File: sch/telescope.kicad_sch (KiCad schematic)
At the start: 74 parts, among them J1 USB_B, J2 M1, J3 M2, J4 12V, J5 UART, Q1 MMBT3904, Q2 MMBT3904, Q3 MMBT3904, SW1 RST, SW2 IO0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

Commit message: split motor driver enable lines and increase motor trace width
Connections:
- net ~{M2_ENA}: now reaches U5.29 (IO5)
- net ~{M2_ENA}: now also U2.23 (~{ENABLE})
- net ~{M_ENA} renamed ~{M1_ENA}
- net ~{M1_ENA}: no longer U2.23 (~{ENABLE})
- no-connect marks 27 -> 26
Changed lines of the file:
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@@
-	)
-	(no_connect
-		(at 236.22 102.87)
 	)
 	(no_connect
@@
 		)
 	)
-	(label "~{M_ENA}"
+	(label "~{M1_ENA}"
 		(at 158.75 52.07 180)
 		(fields_autoplaced yes)
@@
 		)
 	)
+	(label "~{M2_ENA}"
+		(at 236.22 102.87 0)
+		(fields_autoplaced yes)
+		(effects
+			(font
+				(size 1.27 1.27)
+			)
+			(justify left bottom)
+		)
+	)
 	(label "LED"
 		(at 190.5 100.33 0)
@@
 		)
 	)
-	(label "~{M_ENA}"
+	(label "~{M1_ENA}"
 		(at 236.22 123.19 0)
 		(fields_autoplaced yes)
@@
 		)
 	)
-	(label "~{M_ENA}"
+	(label "~{M2_ENA}"
 		(at 231.14 52.07 180)
 		(fields_autoplaced yes)

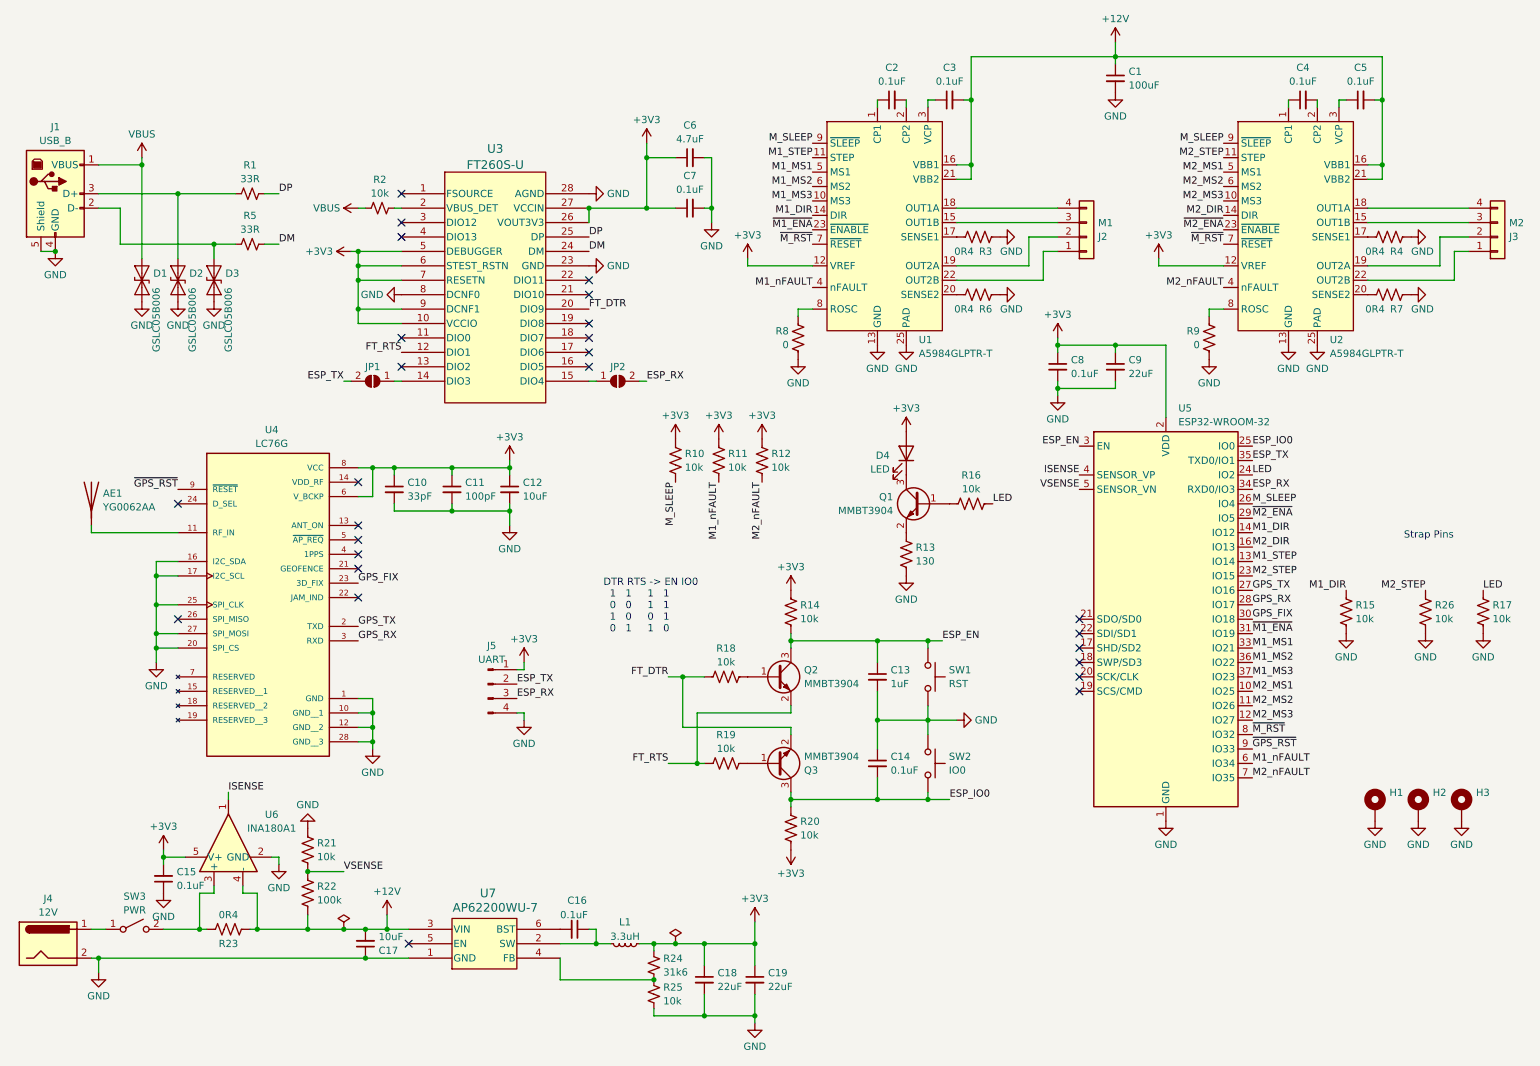
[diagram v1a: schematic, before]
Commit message: add overvolt protection, USB power, and GPO to schematics
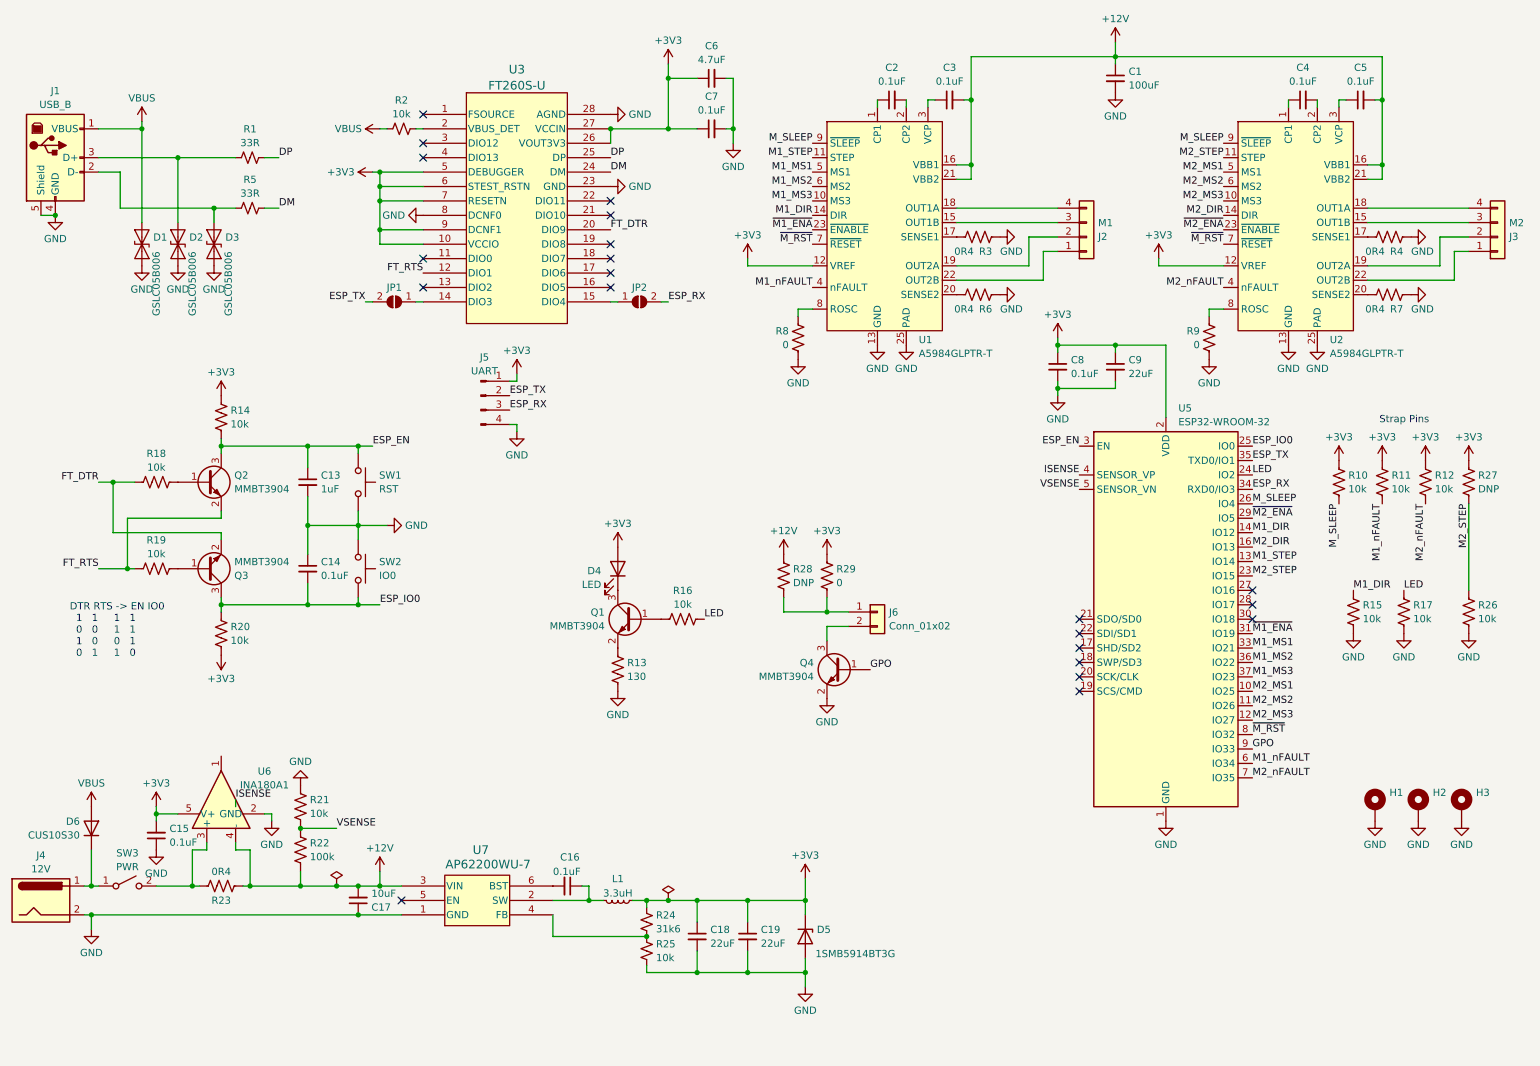
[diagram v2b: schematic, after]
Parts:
- removed AE1: YG0062AA, YG0062AA:XCVR_YG0062AA, symbol Device:Antenna
- removed C10: 33pF, Capacitor_SMD:C_0805_2012Metric_Pad1.18x1.45mm_HandSolder, symbol Device:C_Small
- removed C11: 100pF, Capacitor_SMD:C_0805_2012Metric_Pad1.18x1.45mm_HandSolder, symbol Device:C_Small
- removed C12: 10uF, Capacitor_SMD:C_0805_2012Metric_Pad1.18x1.45mm_HandSolder, symbol Device:C_Small
- removed U4: LC76G, LC76G:XCVR_LC76G, symbol LC76G:LC76G
- added D5: 1SMB5914BT3G, symbol Device:D_Zener
- added D6: CUS10S30, symbol Device:D
- added J6: Conn_01x02, symbol Connector_Generic:Conn_01x02
- added Q4: MMBT3904, Package_TO_SOT_SMD:SOT-23, symbol Transistor_BJT:MMBT3904
- added R27: DNP, Resistor_SMD:R_0805_2012Metric_Pad1.20x1.40mm_HandSolder, symbol Device:R_US
- added R28: DNP, symbol Device:R_US
- added R29: 0, symbol Device:R_US
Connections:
- net +12V: now also R28.1
- net +3V3: now also D5.1 (K), R27.2, R29.1
- net GND: now also D5.2 (A), Q4.2 (E)
- net ISENSE: no longer U6.1
- net M2_STEP: now also R27.1
- net VBUS: now also D6.2 (A)
- net at J4.1, SW3.1 (A): now also D6.1 (K)
- net GPS_FIX: no longer names the net of U5.30 (IO18)
- net GPS_RX: no longer names the net of U5.28 (IO17)
- net GPS_TX: no longer names the net of U5.27 (IO16)
- net ~{GPS_RST} renamed GPO
- net GPO: now also Q4.1 (B)
- new net: J6.1 (Pin_1), R28.2, R29.2
- new net: J6.2 (Pin_2), Q4.3 (C)
- no-connect marks 26 -> 21
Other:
- moved on the sheet: C13, C14, C15, C16, C17, C18, C19, C6, C7, D1, D2, D3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

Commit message: update pcb
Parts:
- removed R29: 0, symbol Device:R_US
- added JP3, JP4: SolderJumper_2_Open, Jumper:SolderJumper-2_P1.3mm_Open_TrianglePad1.0x1.5mm, symbol Jumper:SolderJumper_2_Open
- added RV1: R_Potentiometer_US, Potentiometer_SMD:Potentiometer_Bourns_TC33X_Vertical, symbol Device:R_Potentiometer_US
- added TP1: TestPoint, TestPoint:TestPoint_Pad_D1.5mm, symbol Connector:TestPoint
- D5: value 1SMB5914BT3G -> PDZ3.6B; footprint (none) -> Diode_SMD:D_SOD-323_HandSoldering
- D6: footprint (none) -> Diode_SMD:D_SOD-323_HandSoldering
- J6: footprint (none) -> Connector_PinHeader_2.54mm:PinHeader_1x02_P2.54mm_Vertical
- R28: value DNP -> 10k; footprint (none) -> Resistor_SMD:R_0805_2012Metric_Pad1.20x1.40mm_HandSolder
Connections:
- net +12V: now also JP3.2 (B); no longer R28.1
- net +3V3: now also JP4.2 (B), RV1.1; no longer U1.12 (VREF), U2.12 (VREF)
- net GND: now also RV1.3
- net GPO: now also R28.2, U5.27 (IO16); no longer Q4.1 (B), U5.9 (IO33)
- net ISENSE: now also U6.1
- net at J6.1 (Pin_1): now also JP3.1 (A), JP4.1 (A); no longer R28.2
- new net: RV1.2, TP1.1, U1.12 (VREF), U2.12 (VREF)
- new net: Q4.1 (B), R28.1
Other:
- moved on the sheet: C13, C14, D4, J5, J6, Q1, Q2, Q3, Q4, R13, R14, R16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

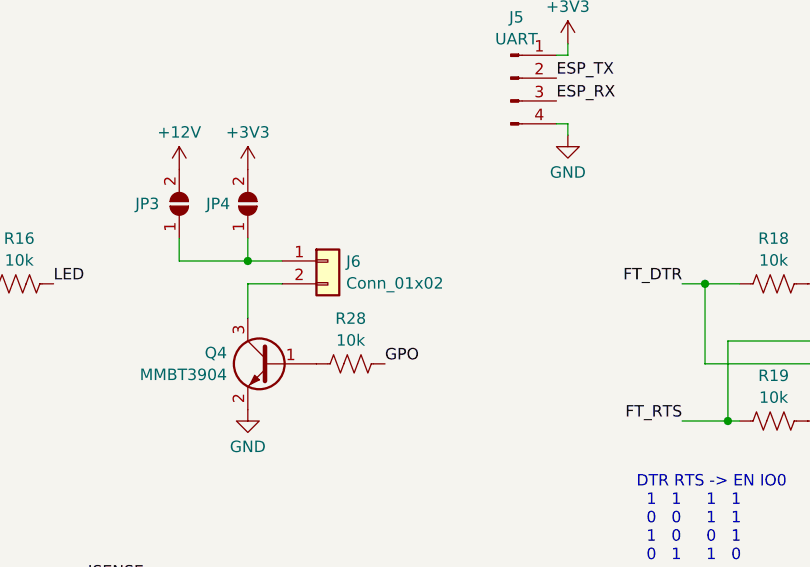
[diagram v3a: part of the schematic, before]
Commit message: switch to jst and generate v2 gerbers
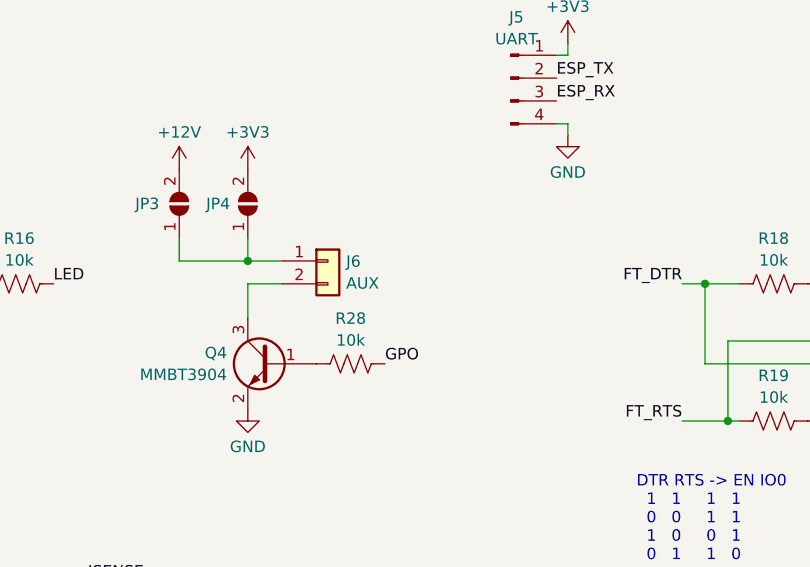
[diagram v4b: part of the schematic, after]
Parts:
- J6: value Conn_01x02 -> AUX; footprint Connector_PinHeader_2.54mm:PinHeader_1x02_P2.54mm_Vertical -> Connector_JST:JST_PH_B2B-PH-K_1x02_P2.00mm_Vertical
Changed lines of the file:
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@@
 			)
 		)
-		(property "Value" "Conn_01x02"
+		(property "Value" "AUX"
 			(at 83.312 110.4321 0)
 			(effects
@@
 			)
 		)
-		(property "Footprint" "Connector_PinHeader_2.54mm:PinHeader_1x02_P2.54mm_Vertical"
+		(property "Footprint" "Connector_JST:JST_PH_B2B-PH-K_1x02_P2.00mm_Vertical"
 			(at 81.28 107.95 0)
 			(effects

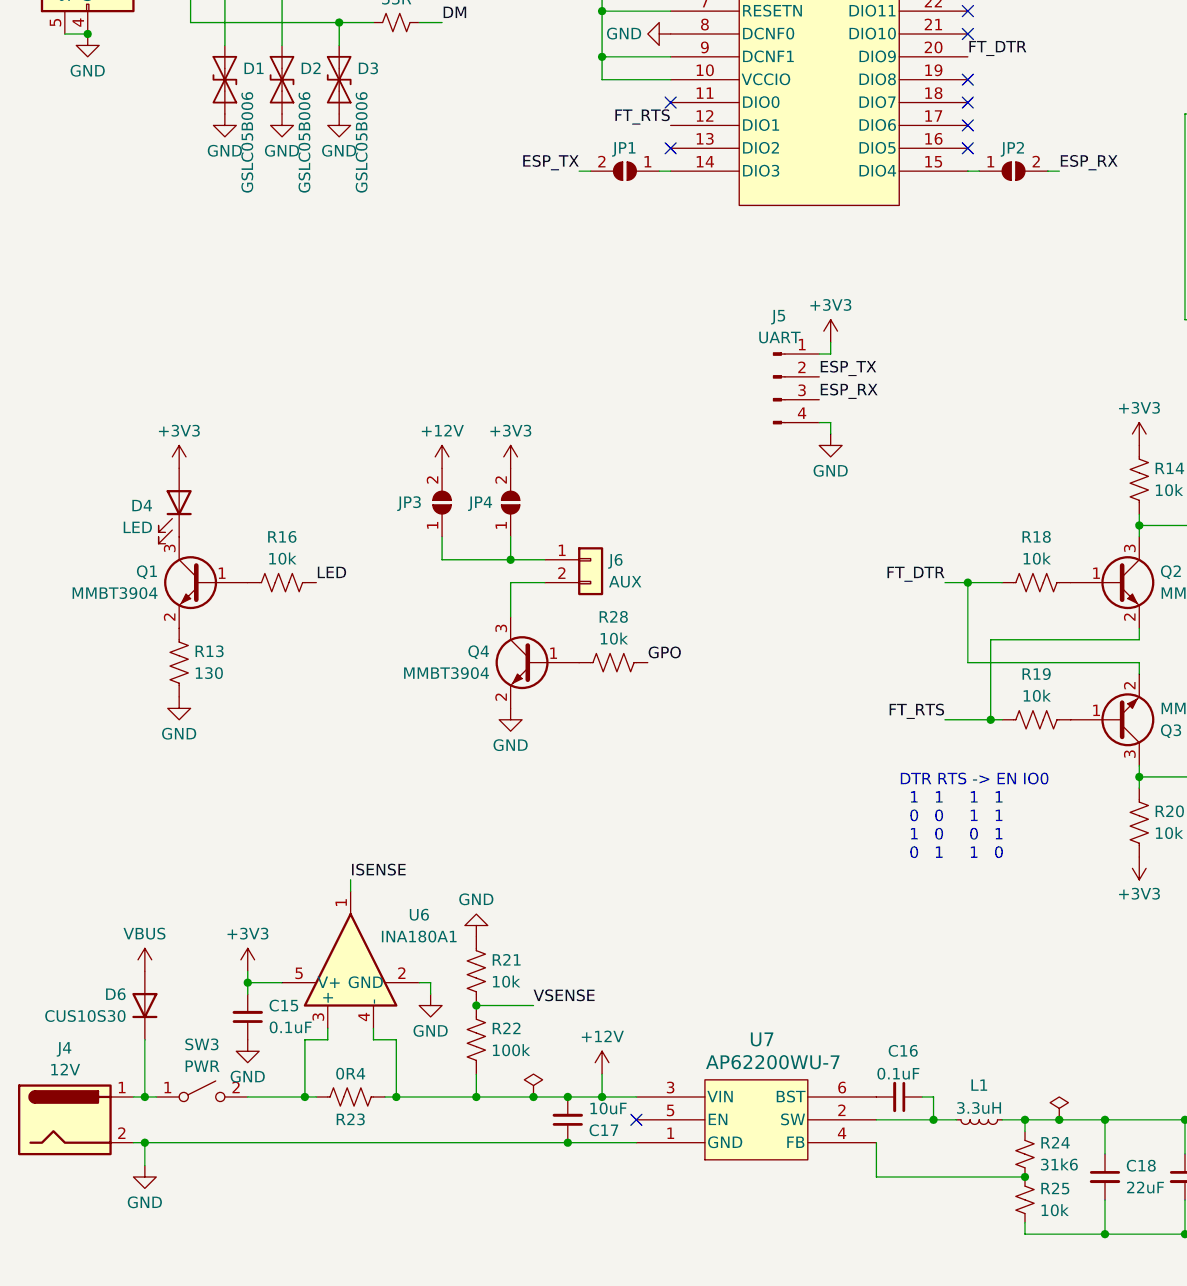
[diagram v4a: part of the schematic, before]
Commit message: add reset control pull down
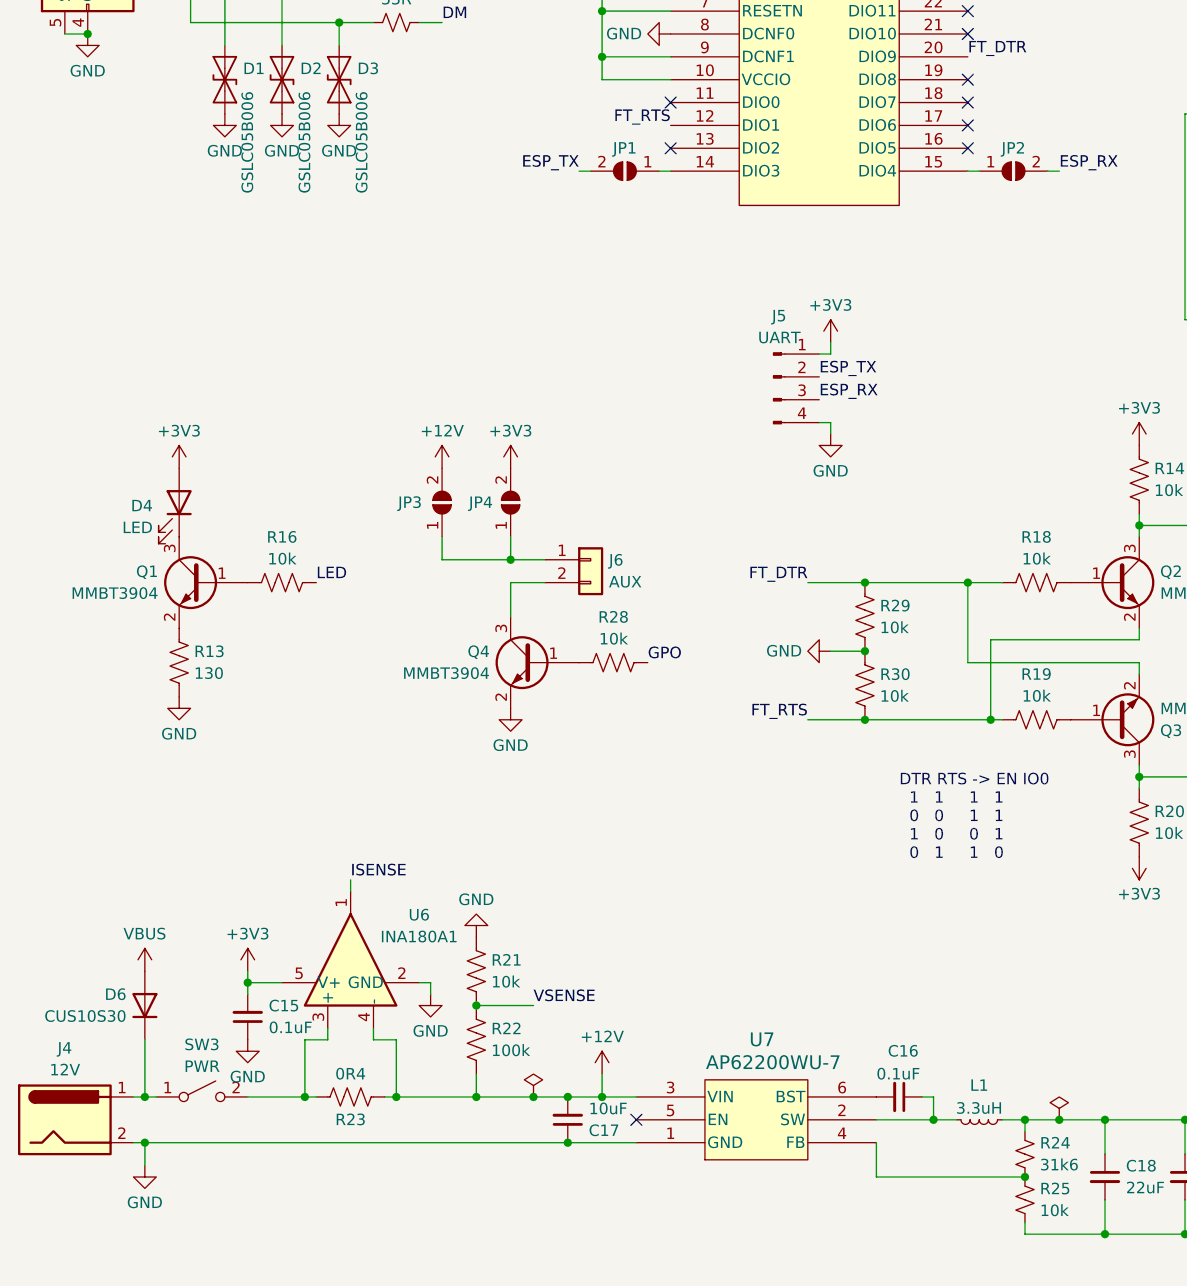
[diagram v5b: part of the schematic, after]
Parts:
- added R29, R30: 10k, Resistor_SMD:R_0805_2012Metric_Pad1.20x1.40mm_HandSolder, symbol Device:R_US
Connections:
- net FT_DTR: now also R29.2
- net FT_RTS: now also R30.1
- net GND: now also R29.1, R30.2
